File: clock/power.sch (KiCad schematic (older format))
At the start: 50 parts, among them U501 TPS56428, U502 TPS56428, U503 TPS56428

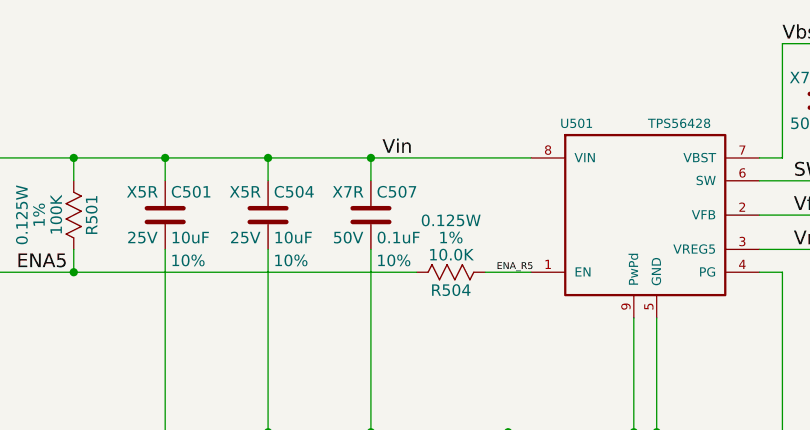
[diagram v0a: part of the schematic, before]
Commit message: Add filter for OCXO power.
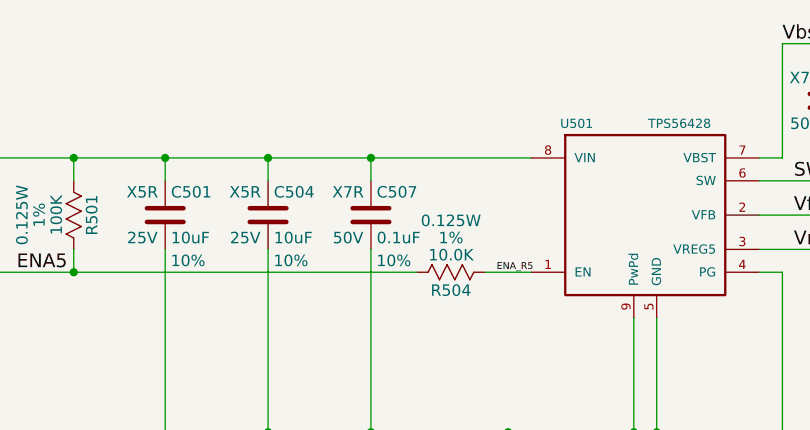
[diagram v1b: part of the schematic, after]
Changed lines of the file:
@@
 Connection ~ 4300 2750
 $Comp
-L GND #PWR074
+L GND #PWR072
 U 1 1 55FF67B4
 P 6200 3650
-F 0 "#PWR074" H 6200 3400 50  0001 C CNN
+F 0 "#PWR072" H 6200 3400 50  0001 C CNN
 F 1 "GND" H 6200 3500 50  0000 C CNN
 F 2 "" H 6200 3650 60  0000 C CNN
@@
 Text Label 6150 2750 0    30   ~ 0
 ENA_R5
-Text Label 5650 2250 0    60   ~ 0
-Vin
 $Comp
 L L L502
@@
 Connection ~ 4300 5350
 $Comp
-L GND #PWR075
+L GND #PWR073
 U 1 1 5619E4B9
 P 6200 6250
-F 0 "#PWR075" H 6200 6000 50  0001 C CNN
+F 0 "#PWR073" H 6200 6000 50  0001 C CNN
 F 1 "GND" H 6200 6100 50  0000 C CNN
 F 2 "" H 6200 6250 60  0000 C CNN
@@
 Connection ~ 4300 7650
 $Comp
-L GND #PWR076
+L GND #PWR074
 U 1 1 561A0FCA
 P 6200 8550
-F 0 "#PWR076" H 6200 8300 50  0001 C CNN
+F 0 "#PWR074" H 6200 8300 50  0001 C CNN
 F 1 "GND" H 6200 8400 50  0000 C CNN
 F 2 "" H 6200 8550 60  0000 C CNN
@@
 GND
 $Comp
-L GND #PWR077
+L GND #PWR075
 U 1 1 563D8E93
 P 3600 8500
-F 0 "#PWR077" H 3600 8250 50  0001 C CNN
+F 0 "#PWR075" H 3600 8250 50  0001 C CNN
 F 1 "GND" H 3600 8350 50  0000 C CNN
 F 2 "" H 3600 8500 60  0000 C CNN

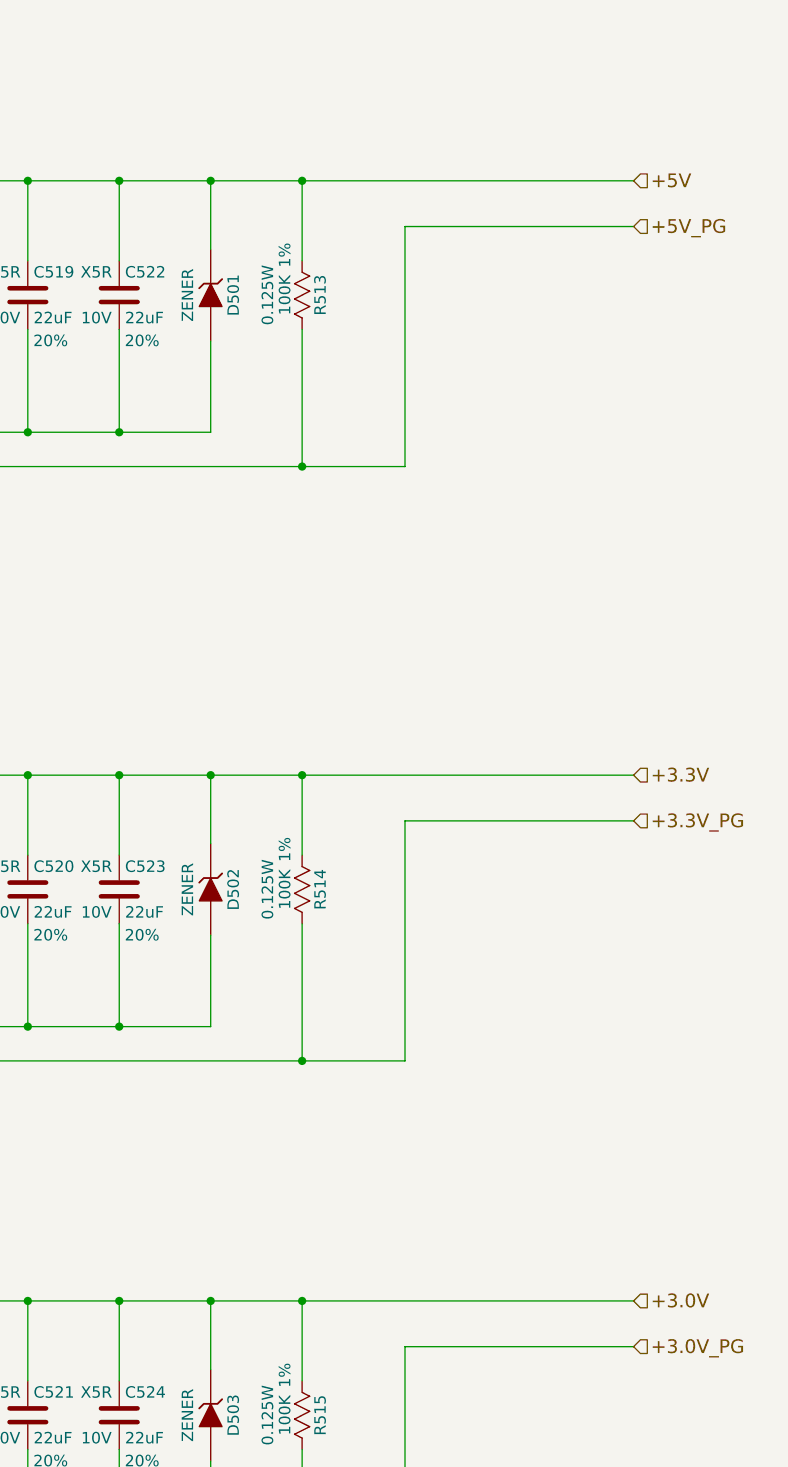
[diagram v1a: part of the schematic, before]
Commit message: Clean up most of the schematic DRC errors. Update placement.
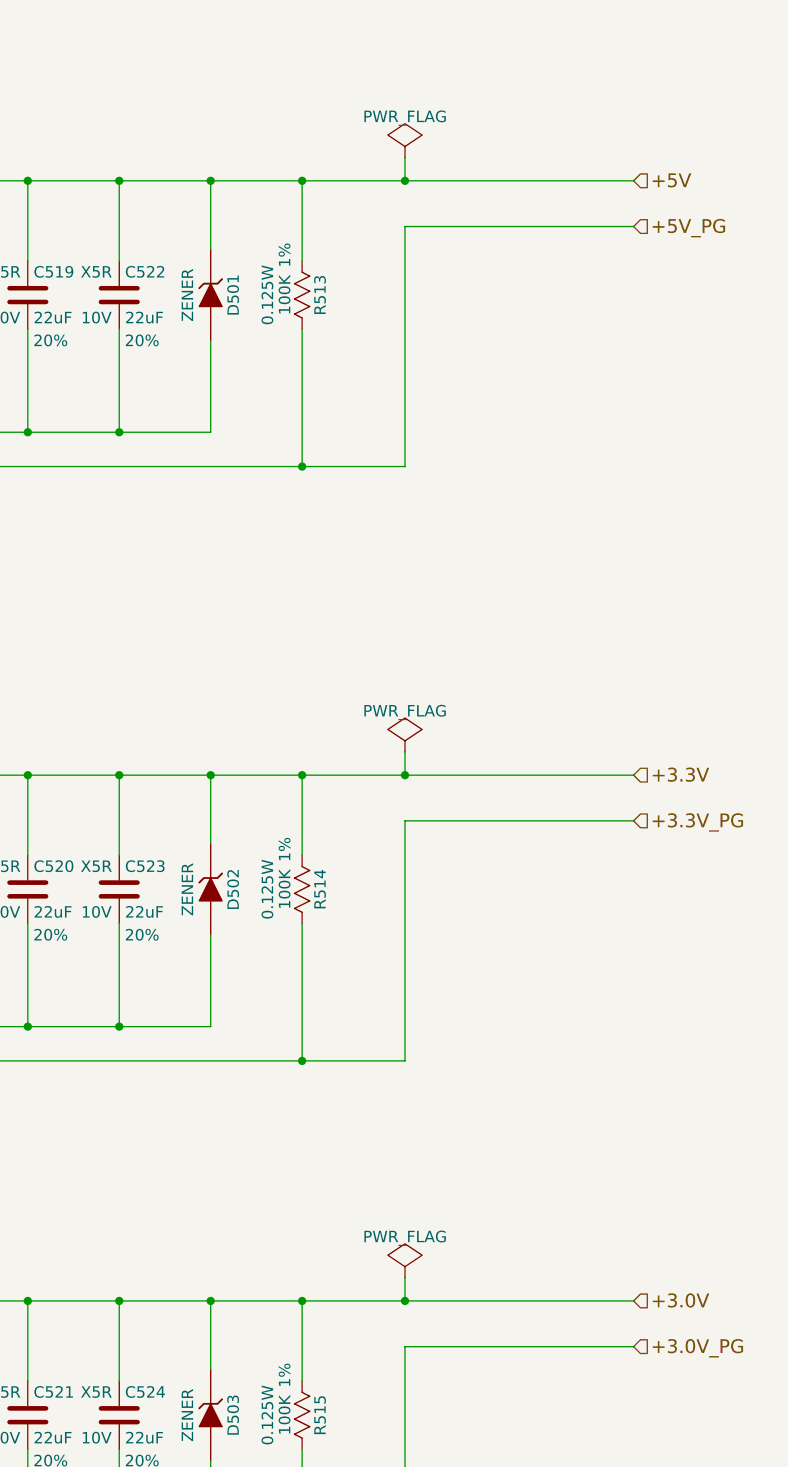
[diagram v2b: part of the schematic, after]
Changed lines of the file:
@@
 Connection ~ 4300 2750
 $Comp
-L GND #PWR072
+L GND #PWR073
 U 1 1 55FF67B4
 P 6200 3650
-F 0 "#PWR072" H 6200 3400 50  0001 C CNN
+F 0 "#PWR073" H 6200 3400 50  0001 C CNN
 F 1 "GND" H 6200 3500 50  0000 C CNN
 F 2 "" H 6200 3650 60  0000 C CNN
@@
 Connection ~ 4300 5350
 $Comp
-L GND #PWR073
+L GND #PWR074
 U 1 1 5619E4B9
 P 6200 6250
-F 0 "#PWR073" H 6200 6000 50  0001 C CNN
+F 0 "#PWR074" H 6200 6000 50  0001 C CNN
 F 1 "GND" H 6200 6100 50  0000 C CNN
 F 2 "" H 6200 6250 60  0000 C CNN
@@
 Connection ~ 4300 7650
 $Comp
-L GND #PWR074
+L GND #PWR075
 U 1 1 561A0FCA
 P 6200 8550
-F 0 "#PWR074" H 6200 8300 50  0001 C CNN
+F 0 "#PWR075" H 6200 8300 50  0001 C CNN
 F 1 "GND" H 6200 8400 50  0000 C CNN
 F 2 "" H 6200 8550 60  0000 C CNN
@@
 GND
 $Comp
-L GND #PWR075
+L GND #PWR076
 U 1 1 563D8E93
 P 3600 8500
-F 0 "#PWR075" H 3600 8250 50  0001 C CNN
+F 0 "#PWR076" H 3600 8250 50  0001 C CNN
 F 1 "GND" H 3600 8350 50  0000 C CNN
 F 2 "" H 3600 8500 60  0000 C CNN
@@
 Wire Wire Line
 	3600 8400 3500 8400
+$Comp
+L PWR_FLAG #FLG077
+U 1 1 56439BF3
+P 11150 2250
+F 0 "#FLG077" H 11150 2345 50  0001 C CNN
+F 1 "PWR_FLAG" H 11150 2430 50  0000 C CNN
+F 2 "" H 11150 2250 60  0000 C CNN
+F 3 "" H 11150 2250 60  0000 C CNN
+	1    11150 2250
+	1    0    0    -1
+$EndComp
+Wire Wire Line
+	11150 2250 11150 2350
+Connection ~ 11150 2350
+$Comp
+L PWR_FLAG #FLG078
+U 1 1 5643A4B3
+P 11150 4850
+F 0 "#FLG078" H 11150 4945 50  0001 C CNN
+F 1 "PWR_FLAG" H 11150 5030 50  0000 C CNN
+F 2 "" H 11150 4850 60  0000 C CNN
+F 3 "" H 11150 4850 60  0000 C CNN
+	1    11150 4850
+	1    0    0    -1
+$EndComp
+Wire Wire Line
+	11150 4850 11150 4950
+Connection ~ 11150 4950
+$Comp
+L PWR_FLAG #FLG079
+U 1 1 5643AC28
+P 11150 7150
+F 0 "#FLG079" H 11150 7245 50  0001 C CNN
+F 1 "PWR_FLAG" H 11150 7330 50  0000 C CNN
+F 2 "" H 11150 7150 60  0000 C CNN
+F 3 "" H 11150 7150 60  0000 C CNN
+	1    11150 7150
+	1    0    0    -1
+$EndComp
+Wire Wire Line
+	11150 7150 11150 7250
+Connection ~ 11150 7250
 $EndSCHEMATC

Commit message: Checkpoint PCB placement.
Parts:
- removed D501, D502, D503: ZENER, Diodes_SMD:SOD-123, symbol ZENER
- L501: Current (none) -> 6.2A; Manufacturer (none) -> TDK; PartNum (none) -> SPM6530T-3R3M
- L502, L503: Current (none) -> 8.4A; Manufacturer (none) -> TDK; PartNum (none) -> SPM6530T-2R2M
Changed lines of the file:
@@
 Comment4 ""
 $EndDescr
-$Comp
-L L L501
-U 1 1 55FF67B2
-P 8200 2350
-F 0 "L501" V 8150 2350 50  0000 C CNN
-F 1 "3.3uH" V 8400 2350 50  0000 C CNN
-F 2 "local:Choke_SMD_7.1x6.5_H3.0_HandSoldering" H 8200 2350 60  0001 C CNN
-F 3 "" H 8200 2350 60  0000 C CNN
-	1    8200 2350
-	0    -1   -1   0
-$EndComp
 Wire Wire Line
 	8500 2350 12150 2350
@@
 Text Label 6150 2750 0    30   ~ 0
 ENA_R5
-$Comp
-L L L502
-U 1 1 5619E46A
-P 8200 4950
-F 0 "L502" V 8150 4950 50  0000 C CNN
-F 1 "2.2uH" V 8400 4950 50  0000 C CNN
-F 2 "local:Choke_SMD_7.1x6.5_H3.0_HandSoldering" H 8200 4950 60  0001 C CNN
-F 3 "" H 8200 4950 60  0000 C CNN
-	1    8200 4950
-	0    -1   -1   0
-$EndComp
 Wire Wire Line
 	8500 4950 12150 4950
@@
 	6750 6050 6750 5550
 Wire Wire Line
-	4700 6050 10300 6050
+	4700 6050 9900 6050
 Wire Wire Line
 	9200 6050 9200 5850
@@
 Text Label 6150 5350 0    30   ~ 0
 ENA_R3.3
-$Comp
-L L L503
-U 1 1 561A0F7B
-P 8200 7250
-F 0 "L503" V 8150 7250 50  0000 C CNN
-F 1 "2.2uH" V 8400 7250 50  0000 C CNN
-F 2 "local:Choke_SMD_7.1x6.5_H3.0_HandSoldering" H 8200 7250 60  0001 C CNN
-F 3 "" H 8200 7250 60  0000 C CNN
-	1    8200 7250
-	0    -1   -1   0
-$EndComp
 Wire Wire Line
 	8500 7250 12150 7250
@@
 	6750 8350 6750 7850
 Wire Wire Line
-	4700 8350 10300 8350
+	4700 8350 9900 8350
 Wire Wire Line
 	9200 8350 9200 8150
@@
 Text Label 6150 7650 0    30   ~ 0
 ENA_R3.0
-Wire Wire Line
-	4700 3450 10300 3450
 Text HLabel 12150 2350 2    60   Input ~ 0
 +5V
@@
 Wire Wire Line
 	11150 7450 11150 8500
-$Comp
-L ZENER D501
-U 1 1 5624EF68
-P 10300 2850
-F 0 "D501" H 10300 2950 50  0000 C CNN
-F 1 "ZENER" H 10300 2750 50  0000 C CNN
-F 2 "Diodes_SMD:SOD-123" H 10300 2850 60  0001 C CNN
-F 3 "" H 10300 2850 60  0000 C CNN
-	1    10300 2850
-	0    1    1    0
-$EndComp
-Wire Wire Line
-	10300 2650 10300 2350
-Connection ~ 10300 2350
-Wire Wire Line
-	10300 3450 10300 3050
-Connection ~ 9900 3450
 Wire Wire Line
 	10700 2700 10700 2350
@@
 Wire Wire Line
 	10700 5600 10700 6200
-$Comp
-L ZENER D502
-U 1 1 56250706
-P 10300 5450
-F 0 "D502" H 10300 5550 50  0000 C CNN
-F 1 "ZENER" H 10300 5350 50  0000 C CNN
-F 2 "Diodes_SMD:SOD-123" H 10300 5450 60  0001 C CNN
-F 3 "" H 10300 5450 60  0000 C CNN
-	1    10300 5450
-	0    1    1    0
-$EndComp
-Wire Wire Line
-	10300 5250 10300 4950
-Wire Wire Line
-	10300 6050 10300 5650
-Connection ~ 9900 6050
 Wire Wire Line
 	10700 7600 10700 7250
 Wire Wire Line
 	10700 7900 10700 8500
-$Comp
-L ZENER D503
-U 1 1 56250BB4
-P 10300 7750
-F 0 "D503" H 10300 7850 50  0000 C CNN
-F 1 "ZENER" H 10300 7650 50  0000 C CNN
-F 2 "Diodes_SMD:SOD-123" H 10300 7750 60  0001 C CNN
-F 3 "" H 10300 7750 60  0000 C CNN
-	1    10300 7750
-	0    1    1    0
-$EndComp
-Wire Wire Line
-	10300 7550 10300 7250
-Wire Wire Line
-	10300 8350 10300 7950
-Connection ~ 9900 8350
 Text HLabel 3500 2750 0    60   Input ~ 0
 +5V_ENA
@@
 	1    0    0    -1
 $EndComp
-Connection ~ 10300 4950
 Connection ~ 10700 4950
 Connection ~ 10700 6200
-Connection ~ 10300 7250
 Connection ~ 10700 7250
 Connection ~ 10700 8500
@@
 	11150 7150 11150 7250
 Connection ~ 11150 7250
+$Comp
+L L L501
+U 1 1 56453093
+P 8200 2350
+F 0 "L501" V 8150 2350 50  0000 C CNN
+F 1 "3.3uH" V 8400 2350 50  0000 C CNN
+F 2 "local:Choke_SMD_7.1x6.5_H3.0_HandSoldering" H 8200 2350 60  0001 C CNN
+F 3 "" V 8150 2350 60  0000 C CNN
+F 4 "6.2A" V 8475 2350 50  0000 C CNN "Current"
+F 5 "TDK" V 8550 2350 50  0001 C CNN "Manufacturer"
+F 6 "SPM6530T-3R3M" V 8625 2350 50  0001 C CNN "PartNum"
+	1    8200 2350
+	0    -1   -1   0
+$EndComp
+$Comp
+L L L502
+U 1 1 56454394
+P 8200 4950
+F 0 "L502" V 8150 4950 50  0000 C CNN
+F 1 "2.2uH" V 8400 4950 50  0000 C CNN
+F 2 "local:Choke_SMD_7.1x6.5_H3.0_HandSoldering" H 8200 4950 60  0001 C CNN
+F 3 "" V 8150 4950 60  0000 C CNN
+F 4 "8.4A" V 8475 4950 50  0000 C CNN "Current"
+F 5 "TDK" V 8550 4950 50  0001 C CNN "Manufacturer"
+F 6 "SPM6530T-2R2M" V 8625 4950 50  0001 C CNN "PartNum"
+	1    8200 4950
+	0    -1   -1   0
+$EndComp
+$Comp
+L L L503
+U 1 1 56454A2E
+P 8200 7250
+F 0 "L503" V 8150 7250 50  0000 C CNN
+F 1 "2.2uH" V 8400 7250 50  0000 C CNN
+F 2 "local:Choke_SMD_7.1x6.5_H3.0_HandSoldering" H 8200 7250 60  0001 C CNN
+F 3 "" V 8150 7250 60  0000 C CNN
+F 4 "8.4A" V 8475 7250 50  0000 C CNN "Current"
+F 5 "TDK" V 8550 7250 50  0001 C CNN "Manufacturer"
+F 6 "SPM6530T-2R2M" V 8625 7250 50  0001 C CNN "PartNum"
+	1    8200 7250
+	0    -1   -1   0
+$EndComp
+Wire Wire Line
+	4700 3450 9900 3450
 $EndSCHEMATC
